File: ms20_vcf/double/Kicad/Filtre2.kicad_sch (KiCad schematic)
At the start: 48 parts, among them J10 Conn_CircuitBoard, J11 Conn_JackBoard, J12 Conn_JackBoard, J13 FilterCV2, J14 FilterIn2, J15 FilterOut2, J9 Conn_CircuitBoard, Q3 BC559, Q4 BC559, SW3 Hpass/Lpass Switch, U3 LM13700, U4 TL072

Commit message: Auto stash before merge of "main" and "origin/main"
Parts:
- Q3, Q4: footprint Package_TO_SOT_THT:TO-92_Inline -> Package_TO_SOT_THT:TO-92_Inline_Wide
- ResLv2, ResVol2: footprint Potentiometer_THT:Potentiometer_Bourns_3386C_Horizontal -> Potentiometer_THT:Potentiometer_Bourns_3386X_Horizontal
- U3: footprint Package_DIP:DIP-16_W7.62mm_Socket -> Package_SO:SOIC-16_3.9x9.9mm_P1.27mm
- renumbered C14 to C15, C11 to C16, C13 to C17, C12 to C18, D12 to D10, D9 to D11, D11 to D12, D10 to D9, J11 to J10, J13 to J11, J15 to J12, J10 to J13, J12 to J14, J14 to J15, R27 to R23, R37 to R24, R23 to R25, R33 to R26, R24 to R27, R32 to R28, R40 to R29, R43 to R30, R25 to R32, R34 to R33, R42 to R34, R41 to R35, R26 to R36, R29 to R37, R35 to R38, R28 to R39, R30 to R40, R38 to R41, R36 to R42, R39 to R43

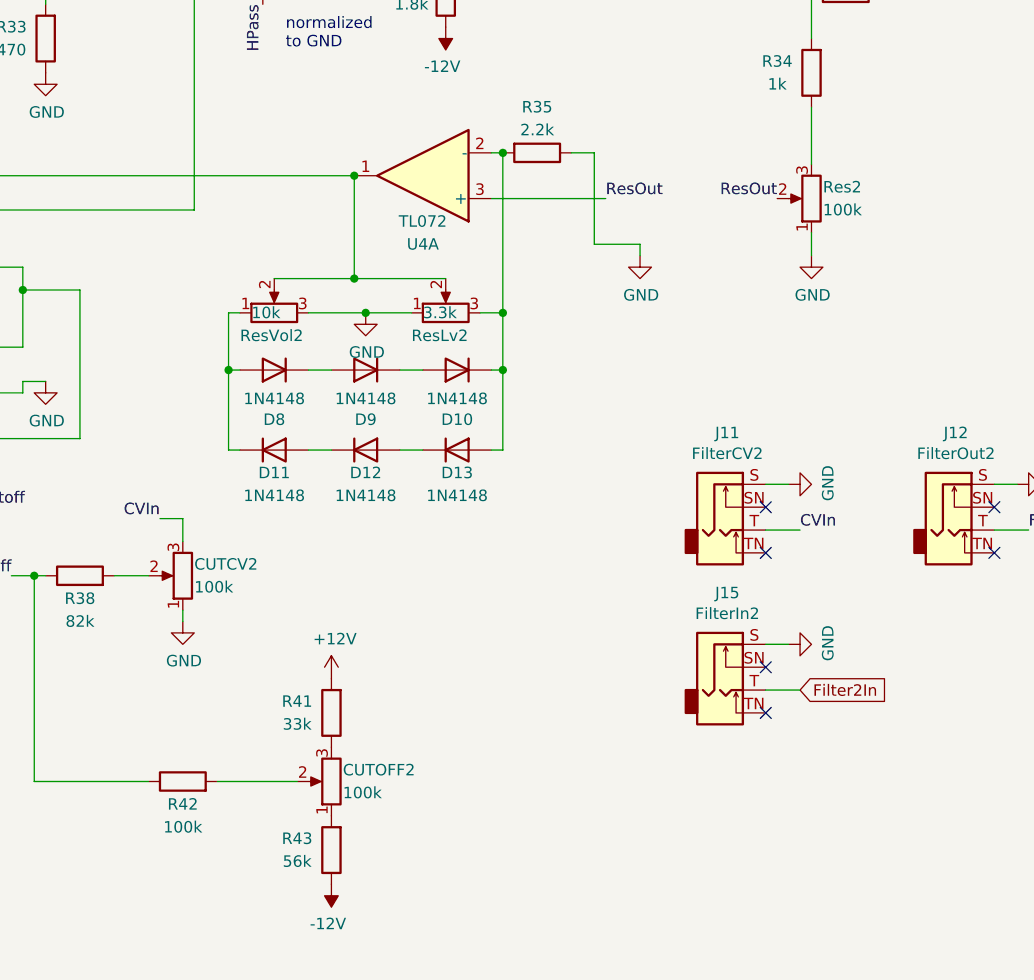
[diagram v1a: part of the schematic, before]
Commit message: updates front panel designs and gerbers before order
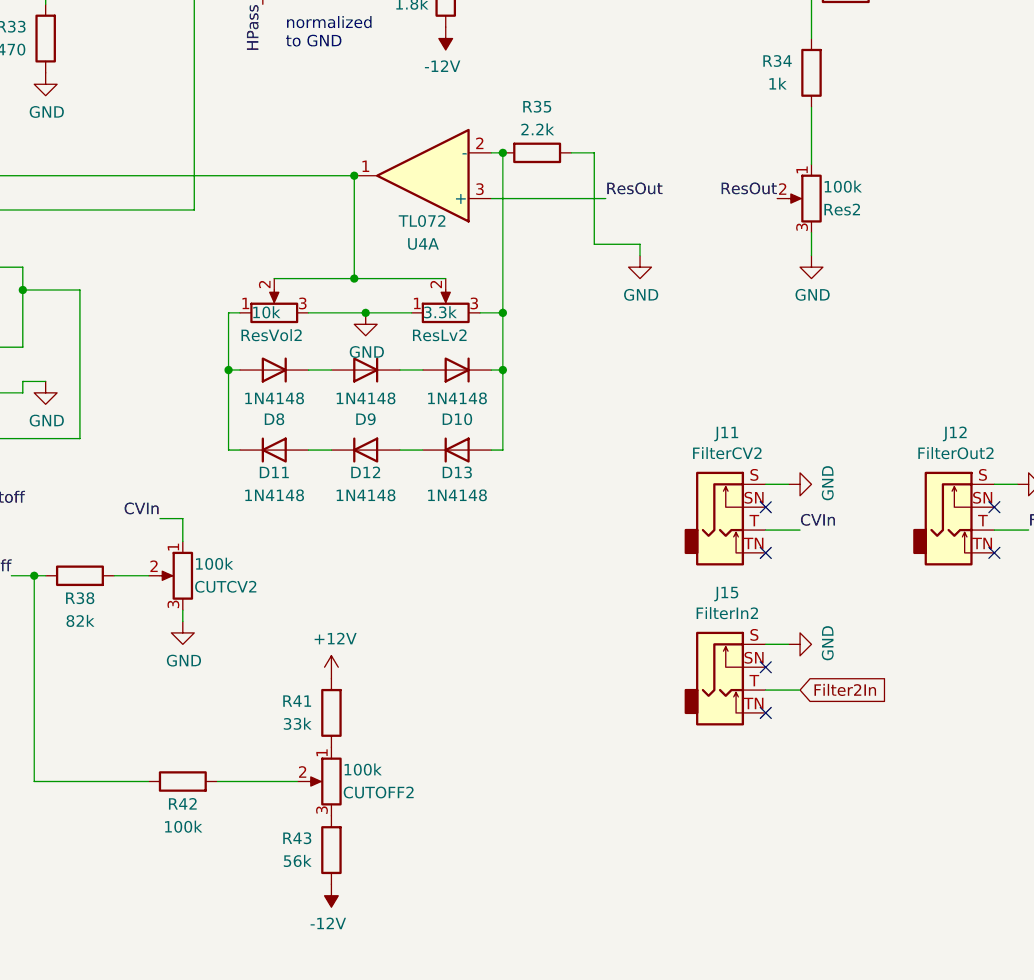
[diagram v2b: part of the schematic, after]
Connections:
- net CVIn: now also CUTCV2.1; no longer CUTCV2.3
- net GND: now also CUTCV2.3, Res2.3; no longer CUTCV2.1, Res2.1
- net at R34.1: now also Res2.1; no longer Res2.3
- net at CUTOFF2.1: now also R41.1; no longer R43.2
- net at CUTOFF2.3: now also R43.2; no longer R41.1
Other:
- moved on the sheet: CUTCV2, CUTOFF2, Res2
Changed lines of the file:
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@@
     (pin "2")
   )
-  (symbol (lib_id "Device:R_POT") (at 236.22 83.82 180) (unit 1)
-    (in_bom yes) (on_board yes)
-    (property "Reference" "Res2" (id 0) (at 237.49 82.55 0)
-      (effects (font (size 1.27 1.27)) (justify right))
-    )
-    (property "Value" "100k" (id 1) (at 237.49 85.09 0)
+  (symbol (lib_id "Device:R_POT") (at 236.22 83.82 0) (mirror y) (unit 1)
+    (in_bom yes) (on_board yes)
+    (property "Reference" "Res2" (id 0) (at 237.49 85.09 0)
+      (effects (font (size 1.27 1.27)) (justify right))
+    )
+    (property "Value" "100k" (id 1) (at 237.49 82.55 0)
       (effects (font (size 1.27 1.27)) (justify right))
     )
@@
     (pin "2")
   )
-  (symbol (lib_id "Device:R_POT") (at 182.88 148.59 180) (unit 1)
-    (in_bom yes) (on_board yes)
-    (property "Reference" "CUTOFF2" (id 0) (at 184.15 147.32 0)
-      (effects (font (size 1.27 1.27)) (justify right))
-    )
-    (property "Value" "100k" (id 1) (at 184.15 149.86 0)
+  (symbol (lib_id "Device:R_POT") (at 182.88 148.59 0) (mirror y) (unit 1)
+    (in_bom yes) (on_board yes)
+    (property "Reference" "CUTOFF2" (id 0) (at 184.15 149.86 0)
+      (effects (font (size 1.27 1.27)) (justify right))
+    )
+    (property "Value" "100k" (id 1) (at 184.15 147.32 0)
       (effects (font (size 1.27 1.27)) (justify right))
     )
@@
     (pin "2")
   )
-  (symbol (lib_id "Device:R_POT") (at 166.37 125.73 180) (unit 1)
-    (in_bom yes) (on_board yes)
-    (property "Reference" "CUTCV2" (id 0) (at 167.64 124.46 0)
-      (effects (font (size 1.27 1.27)) (justify right))
-    )
-    (property "Value" "100k" (id 1) (at 167.64 127 0)
-      (effects (font (size 1.27 1.27)) (justify right))
-    )
+  (symbol (lib_id "Device:R_POT") (at 166.37 125.73 0) (mirror y) (unit 1)
+    (in_bom yes) (on_board yes)
+    (property "Reference" "CUTCV2" (id 0) (at 167.64 127 0)
+      (effects (font (size 1.27 1.27)) (justify right))
+    )
+    (property "Value" "100k" (id 1) (at 167.64 124.46 0)
+      (effects (font (size 1.27 1.27)) (justify right))
+    )
